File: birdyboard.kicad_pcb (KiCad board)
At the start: 4 copper layers, 51 parts, among them J1 JST_3pin, J10 Conn_02x20_Odd_Even, J11 JST-PH StepMotor Conn, J12 TBP02R2-381-04BE, J13 Screw_Terminal_01x02, J14 Screw_Terminal_01x02, J15 Screw_Terminal_01x02, J16 JST-PH StepMotor Conn, J17 TBP02R2-381-04BE, J18 JST-PH StepMotor Conn, J19 TBP02R2-381-04BE, J2 JST_3pin, J20 JST-PH StepMotor Conn, J21 JST-PH UART Conn, J22 TBP02R2-381-04BE, J24 AS5047_Adapter_Board_Connector, J25 AS5047_Adapter_Board_Connector, J26 AS5047_Adapter_Board_Connector, J27 AS5047_Adapter_Board_Connector, J4 JST_3pin, J5 JST_3pin, J6 JST_3pin, J7 JST_3pin, J8 JST_3pin, J9 JST_3pin, U1 TMC2209_SILENTSTEPSTICK, U2 TMC2209_SILENTSTEPSTICK, U3 Pico, U4 TMC2209_SILENTSTEPSTICK, U5 TMC2209_SILENTSTEPSTICK, U6 SN74CBT3253 MUX/DEMUX, U7 AZ1117CH-3_3TRG1, U8 K7805-3AR3

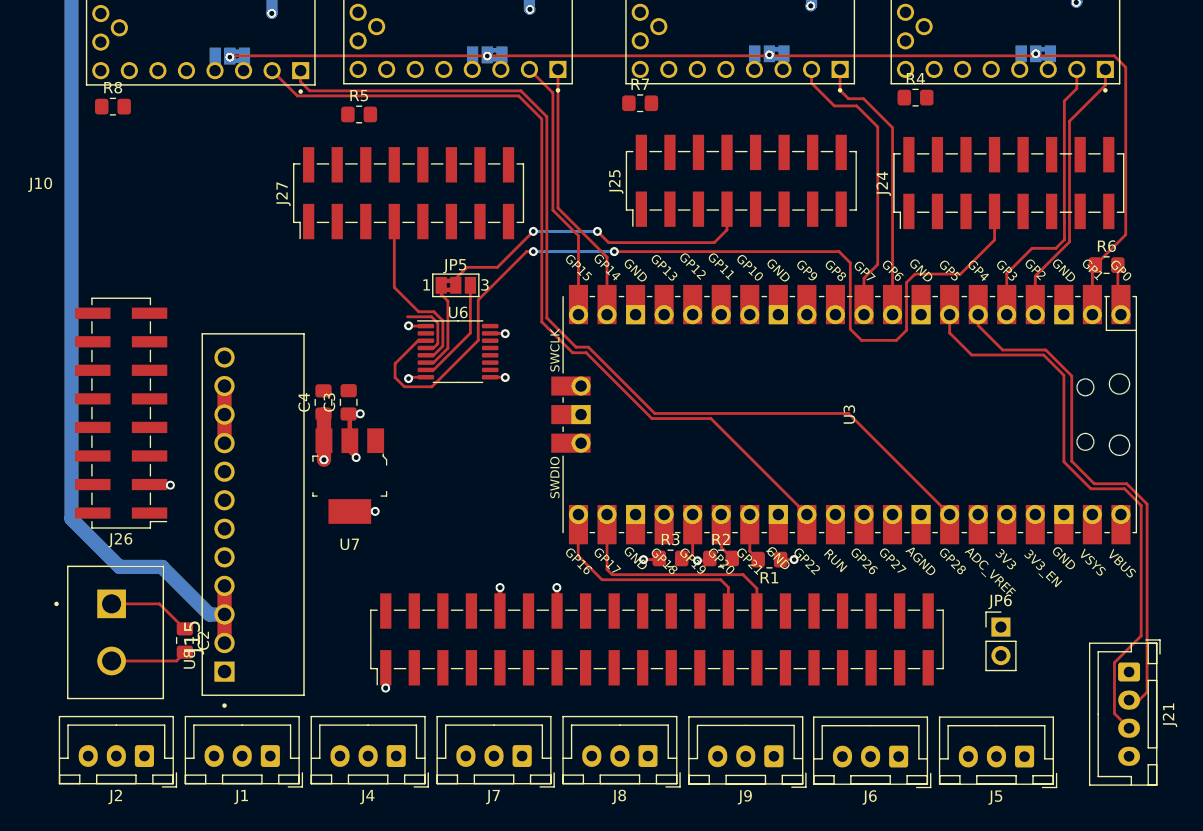
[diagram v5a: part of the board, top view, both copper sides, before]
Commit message: connects up the PCB Layout
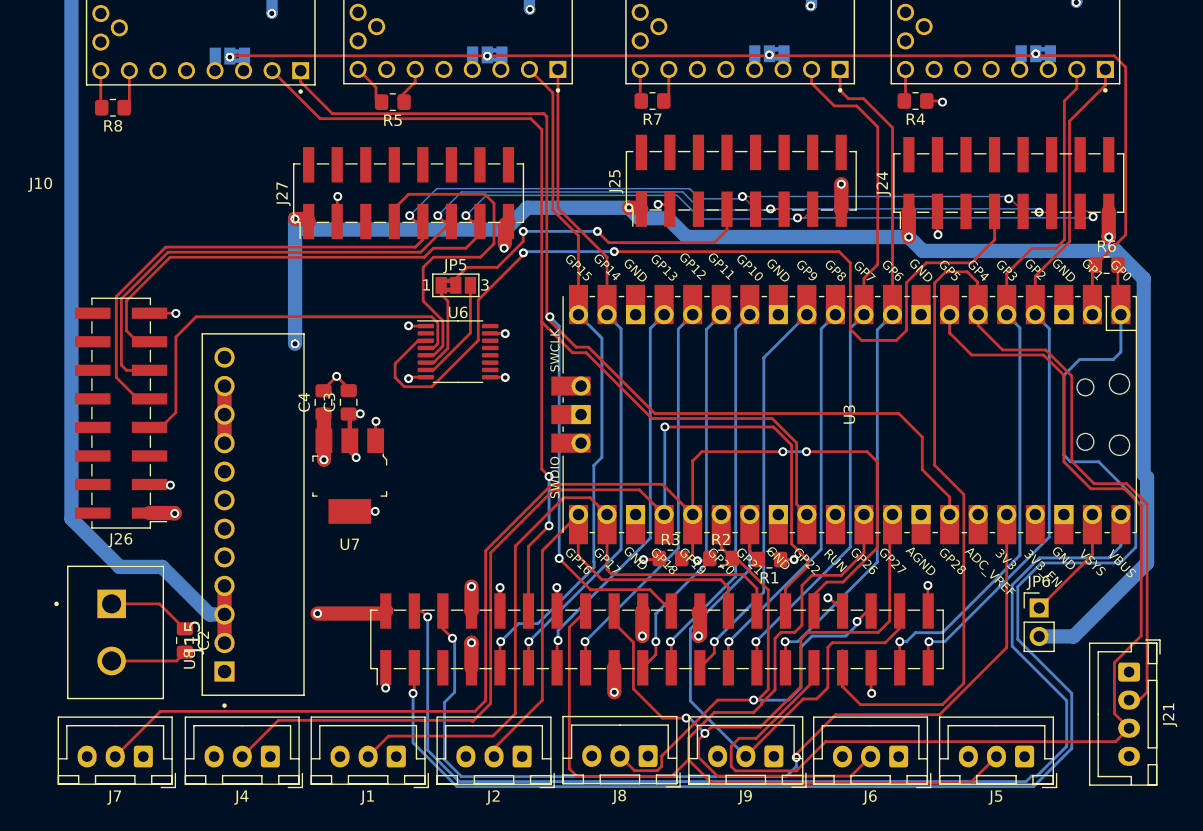
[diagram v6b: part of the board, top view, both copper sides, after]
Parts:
- moved J7 33.7 mm to (80.9, 142.2)
- moved J2 33.6 mm to (114.6, 142.2)
- moved J1 11.2 mm to (103.4, 142.2)
- moved J4 11.2 mm to (92.2, 142.2)
- moved JP6 3.80 mm to (160.6, 129.0)
- moved R5 3.20 mm to (103.1, 84.0), turned to 180 degrees
- moved R7 1.12 mm to (126.2, 83.9), turned to 180 degrees
- moved R4 0.30 mm to (149.6, 83.9), turned to 180 degrees
- moved R8 0.10 mm to (78.2, 84.5), turned to 180 degrees
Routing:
- net +5V: track 16.6 -> 160.2 mm, vias 1 -> 8
- net GPIO0: track 4.52 -> 129.9 mm, vias 0 -> 1
- net GPIO19: track 4.07 -> 112.8 mm, vias 0 -> 2
- net PICO_VBus: track 0.00 -> 102.8 mm, vias 0 -> 1
- net ENC_MISO: track 0.00 -> 102.1 mm, vias 0 -> 3
- net ENC_CLK: track 0.00 -> 101.5 mm, vias 0 -> 3
- net ENC_MOSI: track 0.00 -> 99.8 mm, vias 0 -> 3
- net GPIO18: track 0.00 -> 92.1 mm, vias 0 -> 1
- net GPIO26: track 0.00 -> 88.0 mm
- net PICO_3V3: track 0.00 -> 81.9 mm, vias 0 -> 2
- net GPIO27: track 0.00 -> 67.4 mm, vias 0 -> 2
- net UART_TX: track 45.6 -> 105.3 mm
- net UART_RX: track 50.9 -> 100.7 mm
- net GPIO21: track 4.32 -> 52.1 mm
- net GPIO20: track 4.32 -> 50.8 mm, vias 0 -> 2
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
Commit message: connect up last two power pads
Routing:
- net +5V: track 160.2 -> 170.9 mm, vias 8 -> 7
- net +3.3V: track 64.7 -> 65.5 mm, vias 18 -> 19
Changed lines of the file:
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@@
   (segment (start 150.6 83.9) (end 151.9 83.9) (width 0.25) (layer "F.Cu") (net 28))
   (segment (start 126.7 124.7) (end 126.8 124.6) (width 0.25) (layer "F.Cu") (net 28))
+  (segment (start 111.7625 103.925) (end 111.7625 103.1375) (width 0.25) (layer "F.Cu") (net 28))
   (segment (start 98.15 92.45) (end 98.2 92.4) (width 0.25) (layer "F.Cu") (net 28))
   (segment (start 127.325 93.1) (end 127.75 93.525) (width 0.25) (layer "F.Cu") (net 28))
@@
   (segment (start 127.2 83.9) (end 127.65 83.45) (width 0.25) (layer "F.Cu") (net 28))
   (segment (start 99.17 111.7475) (end 100.1825 111.7475) (width 0.4) (layer "F.Cu") (net 28))
+  (segment (start 111.7625 103.1375) (end 111.8 103.1) (width 0.25) (layer "F.Cu") (net 28))
   (segment (start 83.25 118.02) (end 83.31 118.08) (width 0.4) (layer "F.Cu") (net 28))
   (segment (start 101.52 120.42) (end 101.53 120.41) (width 0.4) (layer "F.Cu") (net 28))
@@
   (via (at 98.2 92.4) (size 0.8) (drill 0.45) (layers "F.Cu" "B.Cu") (net 28))
   (via (at 151.6 95.8) (size 0.8) (drill 0.45) (layers "F.Cu" "B.Cu") (net 28))
+  (via (at 111.8 103.1) (size 0.8) (drill 0.45) (layers "F.Cu" "B.Cu") (net 28))
   (via (at 152 84) (size 0.8) (drill 0.45) (layers "F.Cu" "B.Cu") (net 28))
   (via (at 92.33 76.11) (size 0.8) (drill 0.45) (layers "F.Cu" "B.Cu") (net 28))
@@
   (segment (start 143.8 123.6) (end 143.8 104.125) (width 0.25) (layer "B.Cu") (net 31))
   (segment (start 143.8 104.125) (end 145.015 102.91) (width 0.25) (layer "B.Cu") (net 31))
-  (segment (start 83.66 120.56) (end 83.7 120.6) (width 1.27) (layer "F.Cu") (net 32))
   (segment (start 96.4 129.5) (end 102.245 129.5) (width 1.27) (layer "F.Cu") (net 32))
   (segment (start 82.34 128.64) (end 84.6 130.9) (width 0.25) (layer "F.Cu") (net 32))
@@
   (segment (start 102.245 129.5) (end 102.47 129.275) (width 1.27) (layer "F.Cu") (net 32))
   (segment (start 96.97 111.7975) (end 96.93 111.7575) (width 1.27) (layer "F.Cu") (net 32))
+  (segment (start 83.94 120.56) (end 85.4 119.1) (width 1.27) (layer "F.Cu") (net 32))
   (segment (start 110.1 129.265) (end 110.09 129.275) (width 1.27) (layer "F.Cu") (net 32))
   (segment (start 96.97 114.12) (end 96.97 115.82) (width 1.27) (layer "F.Cu") (net 32))
   (segment (start 125.085 93.4) (end 125.21 93.525) (width 1.27) (layer "F.Cu") (net 32))
   (segment (start 88.125 109.26) (end 88.125 111.8) (width 1.27) (layer "F.Cu") (net 32))
+  (segment (start 85.4 119.1) (end 85.4 114.525) (width 1.27) (layer "F.Cu") (net 32))
+  (segment (start 85.4 114.525) (end 88.125 111.8) (width 1.27) (layer "F.Cu") (net 32))
+  (segment (start 81.455 120.56) (end 83.94 120.56) (width 1.27) (layer "F.Cu") (net 32))
   (segment (start 124.1 93.4) (end 125.085 93.4) (width 1.27) (layer "F.Cu") (net 32))
   (segment (start 94.4 94.4) (end 95.385 94.4) (width 1.27) (layer "F.Cu") (net 32))
   (segment (start 102.5 129.245) (end 102.47 129.275) (width 1.27) (layer "F.Cu") (net 32))
-  (segment (start 81.455 120.56) (end 83.66 120.56) (width 1.27) (layer "F.Cu") (net 32))
   (segment (start 149 93.735) (end 149.01 93.725) (width 1.27) (layer "F.Cu") (net 32))
   (segment (start 110.1 127.1) (end 110.1 129.265) (width 1.27) (layer "F.Cu") (net 32))
@@
   (via (at 110.1 127.1) (size 0.8) (drill 0.45) (layers "F.Cu" "B.Cu") (net 32))
   (via (at 96.97 115.82) (size 0.8) (drill 0.45) (layers "F.Cu" "B.Cu") (net 32))
-  (via (at 83.7 120.6) (size 0.8) (drill 0.45) (layers "F.Cu" "B.Cu") (net 32))
   (via (at 124.1 93.4) (size 0.8) (drill 0.45) (layers "F.Cu" "B.Cu") (net 32))
   (segment (start 170.2 117.4) (end 170.2 125) (width 1.27) (layer "B.Cu") (net 32))

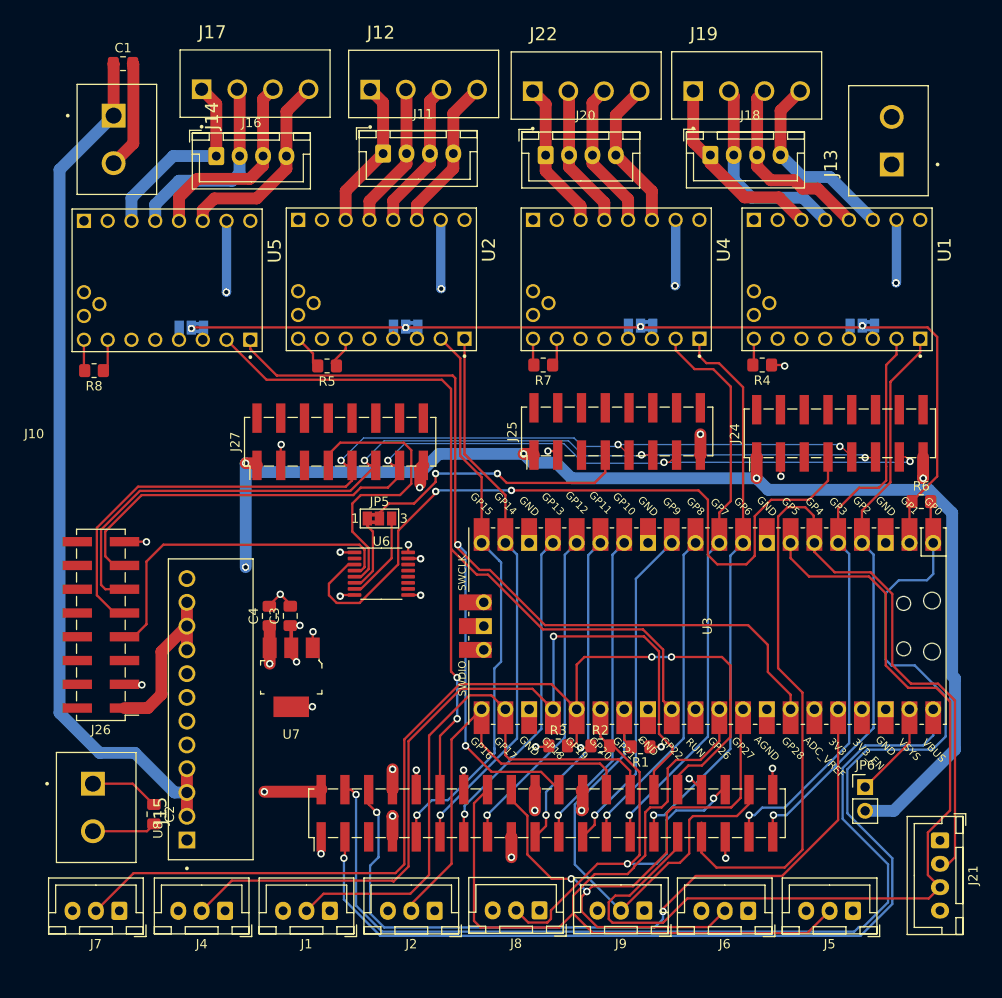
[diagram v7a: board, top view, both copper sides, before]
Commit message: fix errors in DRC
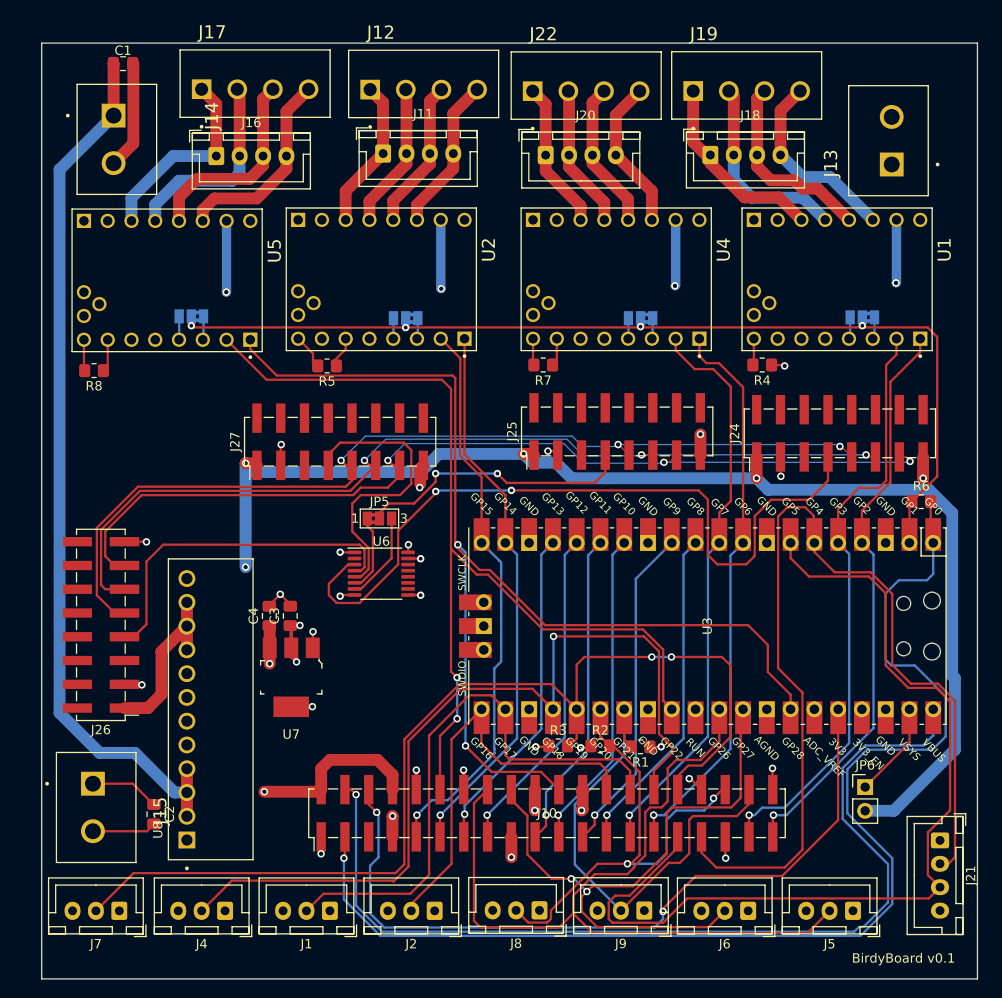
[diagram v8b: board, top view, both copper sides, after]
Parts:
- moved JP4 1.20 mm to (88.6, 78.7)
- moved JP1 0.90 mm to (160.3, 78.8)
- moved JP2 0.90 mm to (111.5, 78.9)
- moved JP3 0.80 mm to (136.6, 78.9)
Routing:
- net +5V: track 170.9 -> 181.2 mm, vias 7 -> 6
- net Net-(JP4-Pad1): track 0.00 -> 2.53 mm
- net Net-(JP4-Pad3): track 0.00 -> 2.51 mm
- net Net-(JP1-Pad1): track 0.00 -> 2.37 mm
- net Net-(JP1-Pad3): track 0.00 -> 2.35 mm
- net Net-(JP3-Pad1): track 0.00 -> 2.23 mm
- net Net-(JP2-Pad1): track 0.00 -> 2.23 mm
- net Net-(JP3-Pad3): track 0.00 -> 2.20 mm
- net UART_TX: track 105.3 -> 103.8 mm
- net Net-(JP2-Pad3): track 0.76 -> 2.20 mm
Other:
- board outline added: 100 x 100 mm
- board text added: "BirdyBoard v0.1"
